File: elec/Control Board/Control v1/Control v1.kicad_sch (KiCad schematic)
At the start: 46 parts, among them J1 DB9_Female_MountingHoles, J10 Conn_02x12_Odd_Even, J11 Screw_Terminal_01x02, J14 Conn_01x08, J2 Conn_01x08, J3 Conn_01x08, J4 Conn_01x08, J5 Conn_01x08, J6 Conn_01x08, J7 Conn_02x18_Odd_Even, J8 Conn_01x10, J9 Conn_01x10

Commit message: Net name congruancy.
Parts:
- removed J14: Conn_01x08, Connector_PinSocket_2.54mm:PinSocket_1x10_P2.54mm_Vertical, symbol Connector_Generic:Conn_01x08
- added J9: Conn_01x10, Connector_PinSocket_2.54mm:PinSocket_1x10_P2.54mm_Vertical, symbol Connector_Generic:Conn_01x10
- added TP103 (x3): GND, TestPoint:TestPoint_Loop_D2.54mm_Drill1.5mm_Beaded, symbol Connector:TestPoint
- A1: footprint PCM_arduino-library:Arduino_Due_Shield -> Arduino:Arduino_Due_Shield
- J10: AssemblyType (none) -> HAND; Distributor 2 (none) -> JLCPCB; Distributor 2 PN (none) -> https://jlcpcb.com/partdetail/Cnjm-CNJMA2006WV_2X12P9T/C283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
- J14: renamed from J9; AssemblyType (none) -> HAND; Cost (none) -> 0.0942; Distributor 1 (none) -> JLCPCB; Distributor 1 PN (none) -> C2894933; MPN (none) -> PZ254-1-10-Z-8.5; Manufacturer (none) -> HCTL
- J2: renamed from J3; AssemblyType (none) -> HAND; Cost (none) -> 0.0762; Distributor 1 (none) -> JLCPCB; Distributor 1 PN (none) -> C2894931; MPN (none) -> PZ254-1-08-Z-8.5; Manufacturer (none) -> HCTL
- J3: renamed from J2; AssemblyType (none) -> HAND; Cost (none) -> 0.0762; Distributor 1 (none) -> JLCPCB; Distributor 1 PN (none) -> C2894931; MPN (none) -> PZ254-1-08-Z-8.5; Manufacturer (none) -> HCTL
- J4, J5, J6: AssemblyType (none) -> HAND; Cost (none) -> 0.0762; Distributor 1 (none) -> JLCPCB; Distributor 1 PN (none) -> C2894931; MPN (none) -> PZ254-1-08-Z-8.5; Manufacturer (none) -> HCTL
- J7: renamed from J8; AssemblyType (none) -> HAND; Cost (none) -> 0.0942; Distributor 1 (none) -> JLCPCB; Distributor 1 PN (none) -> C2894933; MPN (none) -> PZ254-1-10-Z-8.5; Manufacturer (none) -> HCTL
- gave numbers to parts that had none: 1
- renumbered J7 to J8, MF3 to MF4
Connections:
- net D22 is gone; now on net SCL: J2.8 (Pin_8)
- net ACI: now also J10.13 (Pin_13); no longer J10.14 (Pin_14)
- net AUX: now also J10.12 (Pin_12), J10.17 (Pin_17), J10.21 (Pin_21), J9.6 (Pin_6); no longer J10.11 (Pin_11), J10.18 (Pin_18), J10.22 (Pin_22)
- net D23: no longer J2.7 (Pin_7)
- net EN+: now also J10.11 (Pin_11); no longer J10.12 (Pin_12)
- net EN-: now also J10.9 (Pin_9); no longer J10.10 (Pin_10)
- net GND: now also J10.10 (Pin_10), J10.14 (Pin_14), J10.16 (Pin_16), J10.18 (Pin_18), J10.22 (Pin_22), J10.6 (Pin_6), J9.3 (Pin_3), J9.5 (Pin_5), J9.7 (Pin_7), J9.8 (Pin_8), J9.9 (Pin_9), TP103.1, TP103.1, TP103.1; no longer J10.13 (Pin_13), J10.15 (Pin_15), J10.17 (Pin_17), J10.21 (Pin_21), J10.5 (Pin_5), J10.9 (Pin_9)
- net PAR: now also J10.7 (Pin_7); no longer J10.8 (Pin_8)
- net POK: now also J10.5 (Pin_5); no longer J10.6 (Pin_6)
- net RX: now also J10.23 (Pin_23); no longer J10.24 (Pin_24)
- net SDA: now also J2.7 (Pin_7)
- net TX: now also J10.24 (Pin_24); no longer J10.23 (Pin_23)
- net VCI: now also J10.15 (Pin_15); no longer J10.16 (Pin_16)
- net VO+: now also J10.2 (Pin_2), J9.1 (Pin_1); no longer J10.1 (Pin_1)
- net VO-: now also J10.4 (Pin_4), J9.2 (Pin_2); no longer J10.3 (Pin_3)
- net VS+: now also J10.1 (Pin_1); no longer J10.2 (Pin_2)
- net VS-: now also J10.3 (Pin_3); no longer J10.4 (Pin_4)
- net VSET: now also J10.8 (Pin_8), J9.4 (Pin_4); no longer J10.7 (Pin_7)
- net at J10.20 (Pin_20): now also R101.1, J9.10 (Pin_10); no longer R101.2
- net at J10.19 (Pin_19): now also R101.2; no longer R101.1
- net BLOWER_PWM renamed nFAN1_PWM
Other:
- note added: "Due Pin Number Connection Notes * A0 Blower Tachometer * D4 Dallas One-Wire connection to Thermocouple Breakouts * D9 Blower PWM * D18 UART TX Digital Power Supply TF800 RX is Pin 23 Ref: https://assets.alliedelec.com/v1560852133/Datasheets/1d230174086e96b6e4801d1c963649f3.pdf * D19 UART RX, Digital Power Supply TF800 TX is Pin 24 Ref: https://assets.alliedelec.com/v1560852133/Datasheets/1d230174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"
- note added: "NULL MODEM here."
- note removed: "Due Pin Number Connection Notes * A0 Blower Tachometer * D4 Dallas One-Wire connection to Thermocouple Breakouts * D9 Blower PWM ??? D18 Digital Power Supply TF800 Pin 23 This is Serial1 TX https://assets.alliedelec.com/v1560852133/Datasheets/1d230174086e96b6e4801d1c963649f3.pdf ??? D19 Digital Power Supply TF800 Pin 24 This is Serial1 RX https://assets.alliedelec.com/v1560852133/Datasheets/1d230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"
- moved on the sheet: J10, J14, J2, R101

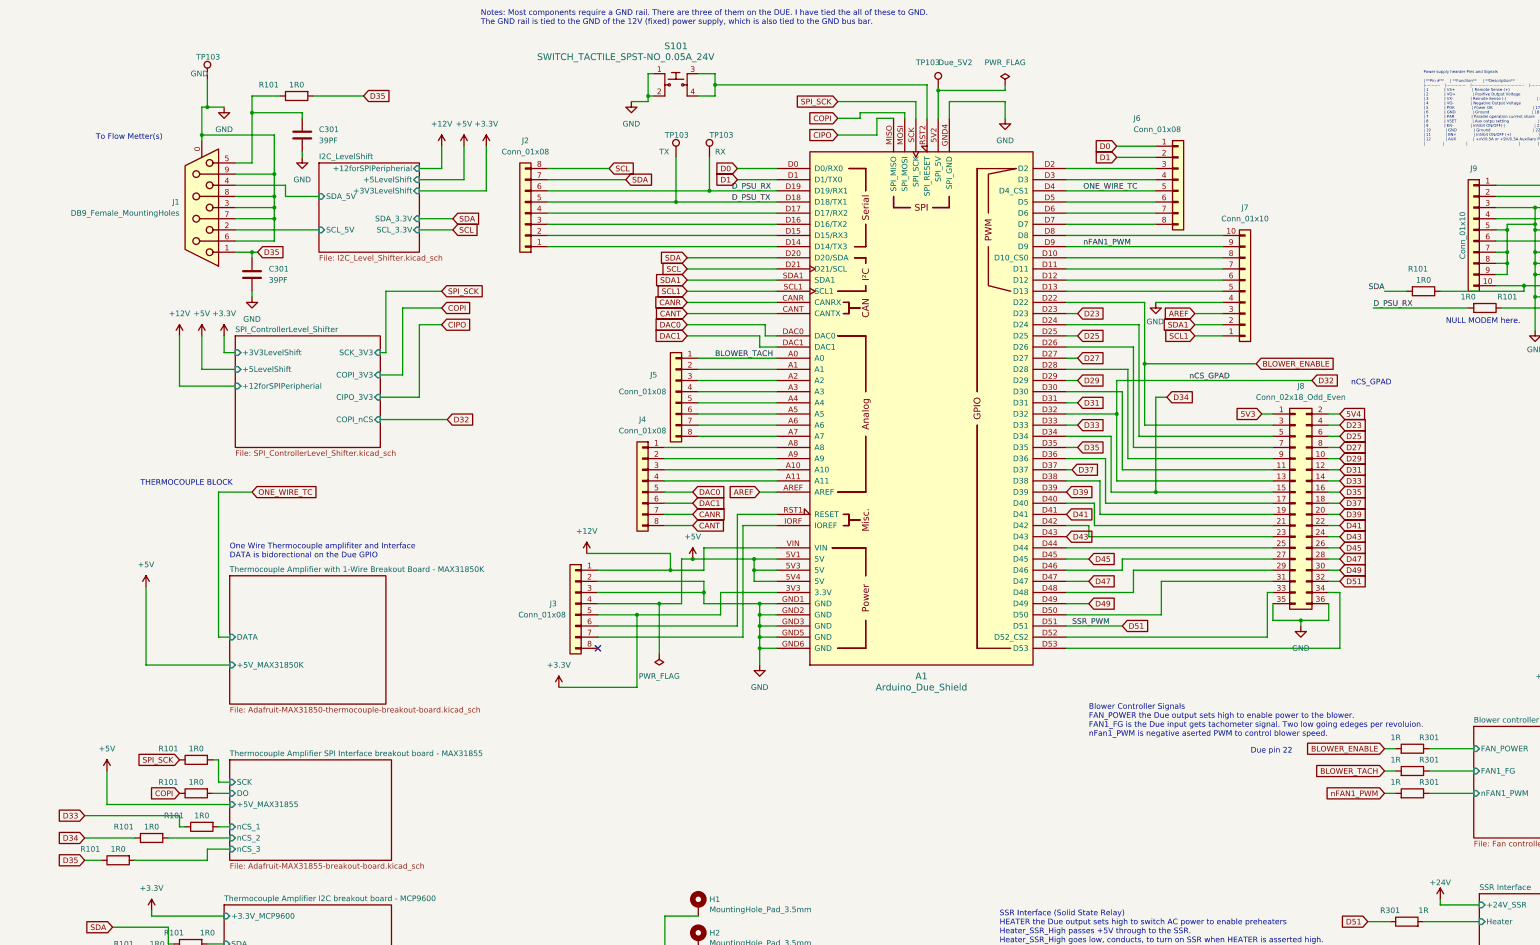
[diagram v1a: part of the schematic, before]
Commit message: Net name congruancy to D35. Add named test points.
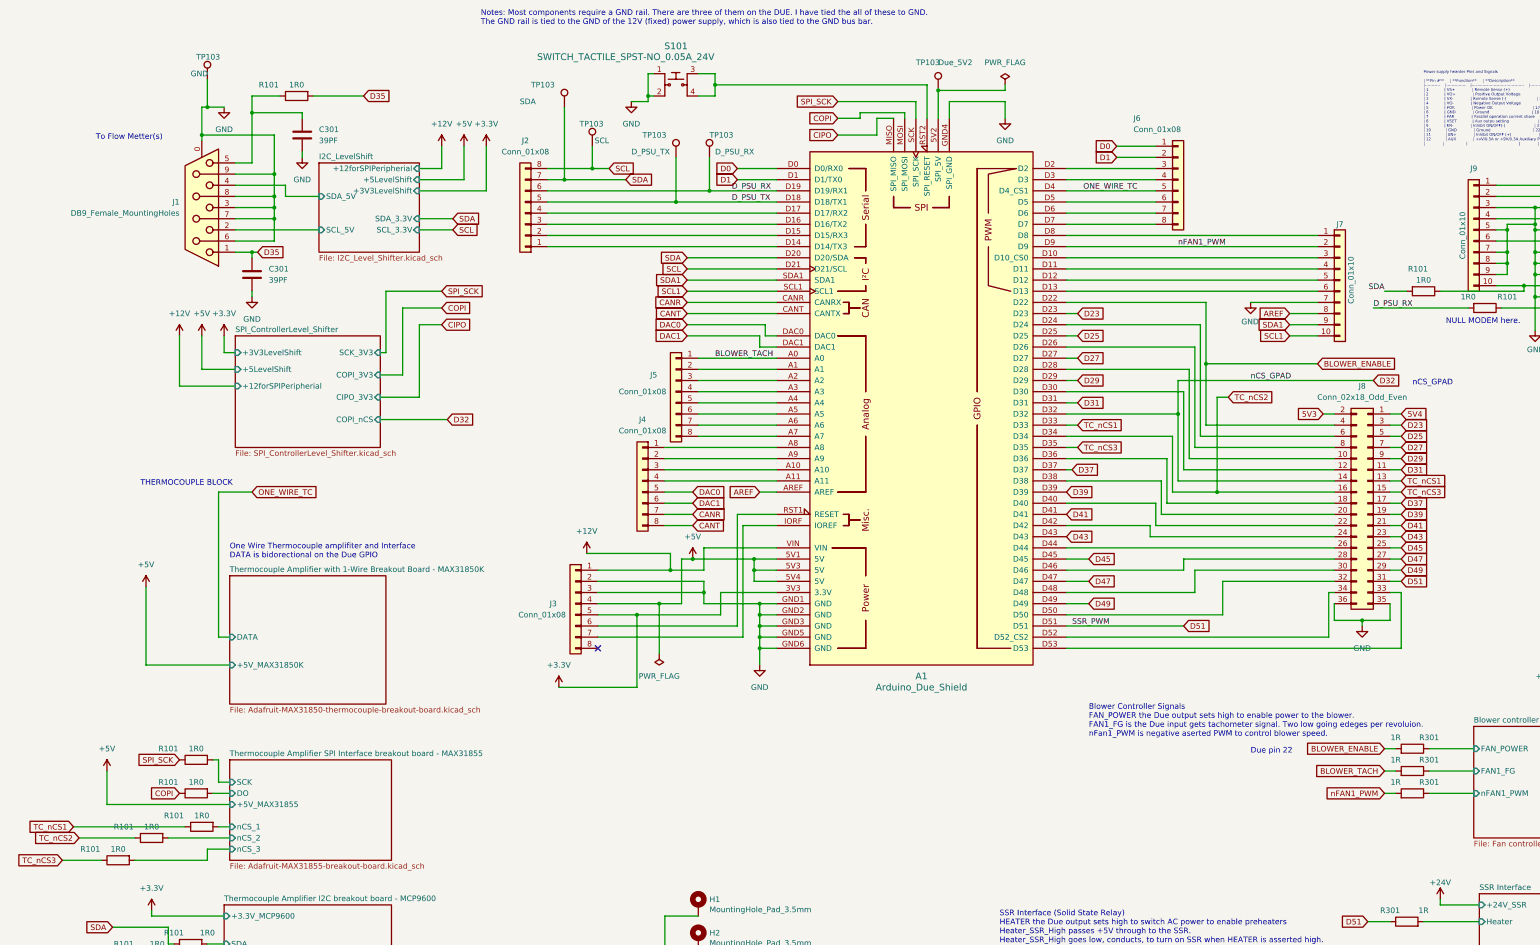
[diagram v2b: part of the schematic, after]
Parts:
- added TP103: SCL, TestPoint:TestPoint_Loop_D2.54mm_Drill1.5mm_Beaded, symbol Connector:TestPoint
- added TP103: SDA, TestPoint:TestPoint_Loop_D2.54mm_Drill1.5mm_Beaded, symbol Connector:TestPoint
- TP103: value TX -> D_PSU_TX
- TP103: value RX -> D_PSU_RX
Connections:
- net 5V3: now also J8.2 (Pin_2); no longer J8.1 (Pin_1)
- net 5V4: now also J8.1 (Pin_1); no longer J8.2 (Pin_2)
- net AREF: now also J7.8 (Pin_8); no longer J7.3 (Pin_3)
- net BLOWER_ENABLE: now also J8.4 (Pin_4); no longer J8.3 (Pin_3)
- net D23: now also J8.3 (Pin_3); no longer J8.4 (Pin_4)
- net D25: now also J8.5 (Pin_5); no longer J8.6 (Pin_6)
- net D27: now also J8.7 (Pin_7); no longer J8.8 (Pin_8)
- net D29: now also J8.9 (Pin_9); no longer J8.10 (Pin_10)
- net D31: now also J8.11 (Pin_11); no longer J8.12 (Pin_12)
- net D32: now also J8.14 (Pin_14); no longer J8.13 (Pin_13)
- net D35: no longer A1.D35, J8.16 (Pin_16), R101.1
- net D37: now also J8.17 (Pin_17); no longer J8.18 (Pin_18)
- net D39: now also J8.19 (Pin_19); no longer J8.20 (Pin_20)
- net D41: now also J8.21 (Pin_21); no longer J8.22 (Pin_22)
- net D43: now also J8.23 (Pin_23); no longer J8.24 (Pin_24)
- net D45: now also J8.25 (Pin_25); no longer J8.26 (Pin_26)
- net D47: now also J8.27 (Pin_27); no longer J8.28 (Pin_28)
- net D49: now also J8.29 (Pin_29); no longer J8.30 (Pin_30)
- net D51: now also J8.31 (Pin_31); no longer J8.32 (Pin_32)
- net GND: now also J7.7 (Pin_7); no longer J7.4 (Pin_4)
- net SCL: now also TP103.1
- net SCL1: now also J7.10 (Pin_10); no longer J7.1 (Pin_1)
- net SDA: now also TP103.1
- net SDA1: now also J7.9 (Pin_9); no longer J7.2 (Pin_2)
- net nFAN1_PWM: now also J7.2 (Pin_2); no longer J7.9 (Pin_9)
- net at A1.D30: now also J8.12 (Pin_12); no longer J8.11 (Pin_11)
- net at A1.D36: now also J8.18 (Pin_18); no longer J8.17 (Pin_17)
- net at A1.D38: now also J8.20 (Pin_20); no longer J8.19 (Pin_19)
- net at A1.D40: now also J8.22 (Pin_22); no longer J8.21 (Pin_21)
- net at A1.D42: now also J8.24 (Pin_24); no longer J8.23 (Pin_23)
- net at A1.D44: now also J8.26 (Pin_26); no longer J8.25 (Pin_25)
- net at A1.D46: now also J8.28 (Pin_28); no longer J8.27 (Pin_27)
- net at A1.D48: now also J8.30 (Pin_30); no longer J8.29 (Pin_29)
- net at A1.D50: now also J8.32 (Pin_32); no longer J8.31 (Pin_31)
- net at J8.33 (Pin_33): now also A1.D53; no longer A1.D52 (D52_CS2)
- net at J8.34 (Pin_34): now also A1.D52 (D52_CS2); no longer A1.D53
- net at A1.D24: now also J8.6 (Pin_6); no longer J8.5 (Pin_5)
- net at A1.D26: now also J8.8 (Pin_8); no longer J8.7 (Pin_7)
- net at A1.D28: now also J8.10 (Pin_10); no longer J8.9 (Pin_9)
- net at A1.D10 (D10_CS0): now also J7.3 (Pin_3); no longer J7.8 (Pin_8)
- net at A1.D11: now also J7.4 (Pin_4); no longer J7.7 (Pin_7)
- net at A1.D12: now also J7.5 (Pin_5); no longer J7.6 (Pin_6)
- net at A1.D13: now also J7.6 (Pin_6); no longer J7.5 (Pin_5)
- net at A1.D8: now also J7.1 (Pin_1); no longer J7.10 (Pin_10)
- net D33 renamed TC_nCS1
- net TC_nCS1: now also J8.13 (Pin_13); no longer J8.14 (Pin_14)
- net D34 renamed TC_nCS2
- net TC_nCS2: now also J8.16 (Pin_16); no longer J8.15 (Pin_15)
- new net TC_nCS3: A1.D35, J8.15 (Pin_15), R101.1
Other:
- moved on the sheet: J7, J8

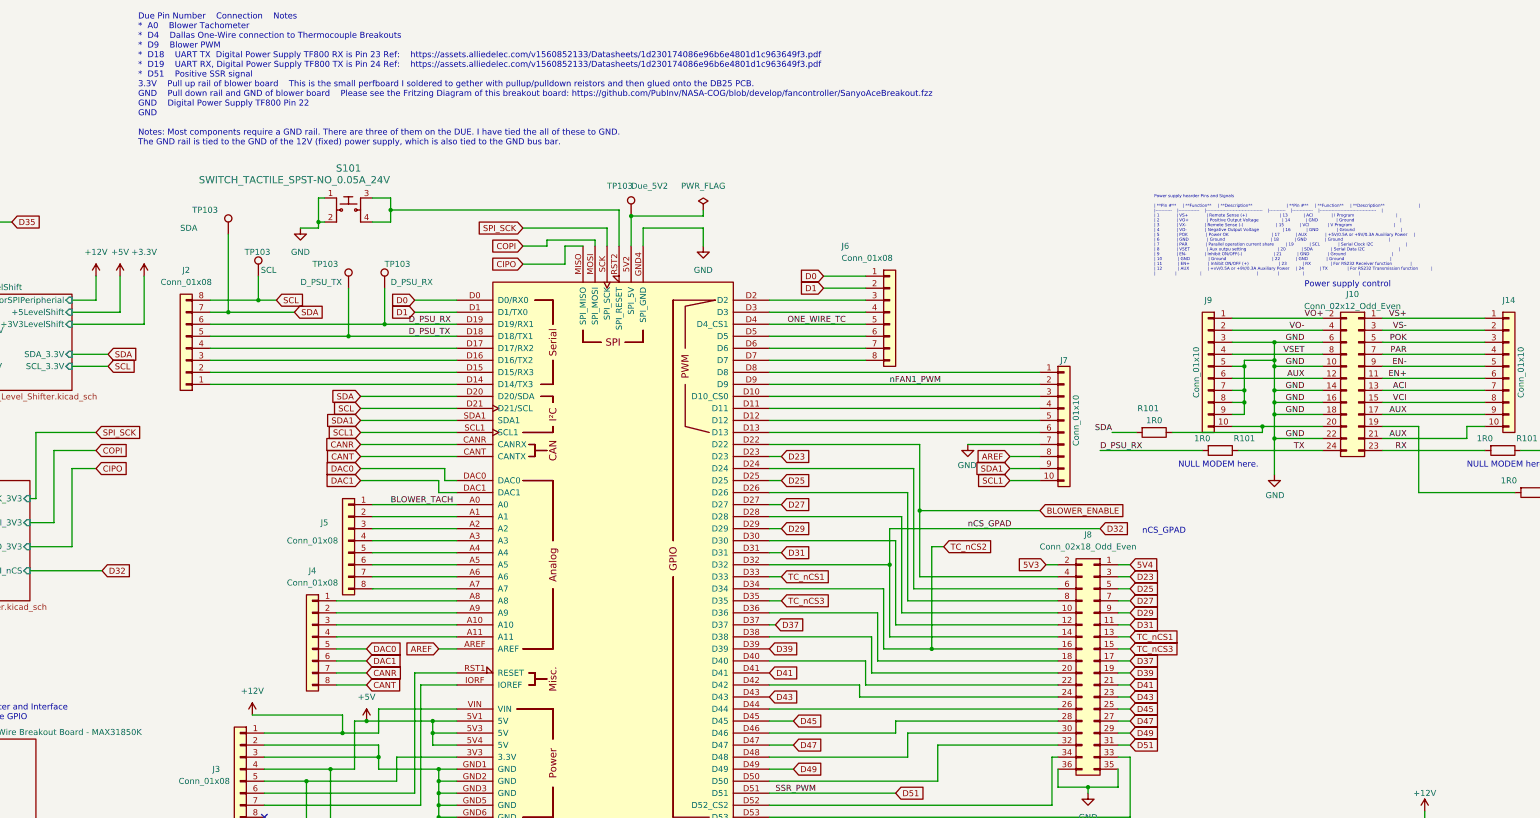
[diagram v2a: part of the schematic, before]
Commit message: Add pull up to I2C. Add test points to SPI.
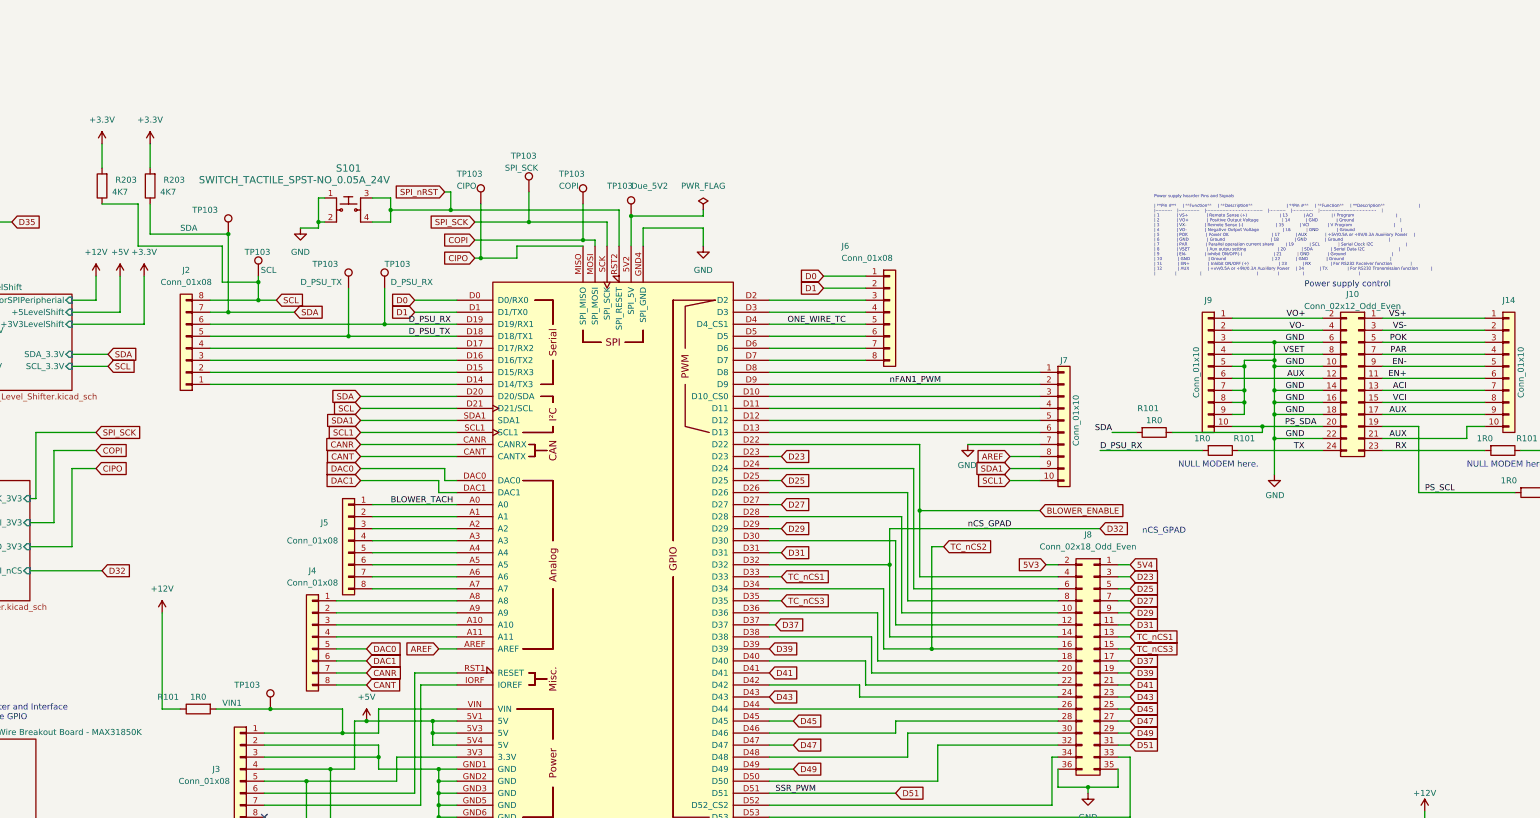
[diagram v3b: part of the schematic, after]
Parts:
- added R101: 1R0, Resistor_SMD:R_0603_1608Metric_Pad0.98x0.95mm_HandSolder, symbol Device:R
- added R203 (x2): 4K7, Resistor_SMD:R_0603_1608Metric_Pad0.98x0.95mm_HandSolder, symbol Device:R
- added TP103: SPI_SCK, TestPoint:TestPoint_Loop_D2.54mm_Drill1.5mm_Beaded, symbol Connector:TestPoint
- added TP103: VIN1, TestPoint:TestPoint_Loop_D2.54mm_Drill1.5mm_Beaded, symbol Connector:TestPoint
- added TP103: COPI, TestPoint:TestPoint_Loop_D2.54mm_Drill1.5mm_Beaded, symbol Connector:TestPoint
- added TP103: CIPO, TestPoint:TestPoint_Loop_D2.54mm_Drill1.5mm_Beaded, symbol Connector:TestPoint
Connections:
- net +12V: now also R101.1; no longer A1.VIN, J3.1 (Pin_1)
- net +3.3V: now also R203.2, R203.2
- net CIPO: now also TP103.1
- net COPI: now also TP103.1
- net SCL: now also R203.1
- net SDA: now also R203.1
- net SPI_SCK: now also TP103.1
- net PS_SDA: now reaches J10.20 (Pin_20), J9.10 (Pin_10), R101.1
- net SPI_nRST: now reaches A1.RST2 (SPI_RESET), S101.3, S101.4
- net PS_SCL: now reaches J10.19 (Pin_19), R101.2
- new net: A1.VIN, J3.1 (Pin_1), R101.2, TP103.1
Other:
- note removed: "Due Pin Number Connection Notes * A0 Blower Tachometer * D4 Dallas One-Wire connection to Thermocouple Breakouts * D9 Blower PWM * D18 UART TX Digital Power Supply TF800 RX is Pin 23 Ref: https://assets.alliedelec.com/v1560852133/Datasheets/1d230174086e96b6e4801d1c963649f3.pdf * D19 UART RX, Digital Power Supply TF800 TX is Pin 24 Ref: https://assets.alliedelec.com/v1560852133/Datasheets/1d230174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"

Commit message: Changes during team review.
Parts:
- added C104: 10nF, Capacitor_SMD:C_0603_1608Metric_Pad1.08x0.95mm_HandSolder, symbol Device:C
- added ISO1, ISO2, ISO3, ISO4, ISO5: MountingHole_Pad_3.5mm, PubInv_KiCad_PCB:MountingHole_3.5mm_Pad_Via, symbol GPAD_SCH_LIB:MountingHole_Pad_3.5mm
- added J25: Screw_Terminal_01x02, TerminalBlock_TE-Connectivity:TerminalBlock_TE_282834-2_1x02_P2.54mm_Horizontal, symbol Connector:Screw_Terminal_01x02
- added R101 (x2): 1R0, Resistor_SMD:R_0603_1608Metric_Pad0.98x0.95mm_HandSolder, symbol Device:R
- added R101: 4M7, Resistor_SMD:R_0603_1608Metric_Pad0.98x0.95mm_HandSolder, symbol Device:R
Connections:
- net GND: now also C104.1, R101.1
- net ONE_WIRE_TC: now also A1.D5, J6.6 (Pin_6); no longer A1.D4 (D4_CS1), J6.5 (Pin_5)
- net VO+: now also R101.2
- net VO-: now also R101.2
- net VS+: now also J25.1 (Pin_1), R101.1, R101.1
- net VS-: now also J25.2 (Pin_2)
- new net: C104.2, ISO1.1, ISO2.1, ISO3.1, ISO4.1, ISO5.1, R101.2
- new net: A1.D4 (D4_CS1), J6.5 (Pin_5)
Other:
- sheet SSR Interface ports: added +12V_SSR; removed none
- sheet Thermocouple Amplifier SPI Interface breakout board - MAX31855  ports: added +3V3_MAX31855; removed none
- sheet Thermocouple Amplifier with 1-Wire Breakout Board - MAX31850K ports: added +3V3_MAX31850K; removed none
- note added: "Power supply hearder Pins and Signals | **Pin #** | **Function** | **Description** | **Pin #** | **Function** | **Description** | |----------- |-------------- |-------------------------------------- |----------- |-------------- |-------------------------------------- | | 1 | VS+ | Remote Sense (+) | 13 | ACI | I Program | | 2 | VO+ | Positive Output Voltage | 14 | GND | Ground | | 3 | VS- | Remot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"
- note added: "Remote Sense"
- note removed: "Power supply hearder Pins and Signals | **Pin #** | **Function** | **Description** | **Pin #** | **Function** | **Description** | |----------- |-------------- |-------------------------------------- |----------- |-------------- |-------------------------------------- | | 1 | VS+ | Remote Sense (+) | 13 | ACI | I Program | | 2 | VO+ | Positive Output Voltage | 14 | GND | Ground | | 3 | VX- | Remot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"
- moved on the sheet: H1, H2, H3, H4, H5, R101, R301
